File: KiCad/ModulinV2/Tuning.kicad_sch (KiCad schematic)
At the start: 35 parts, among them IC51 TL074HIDR

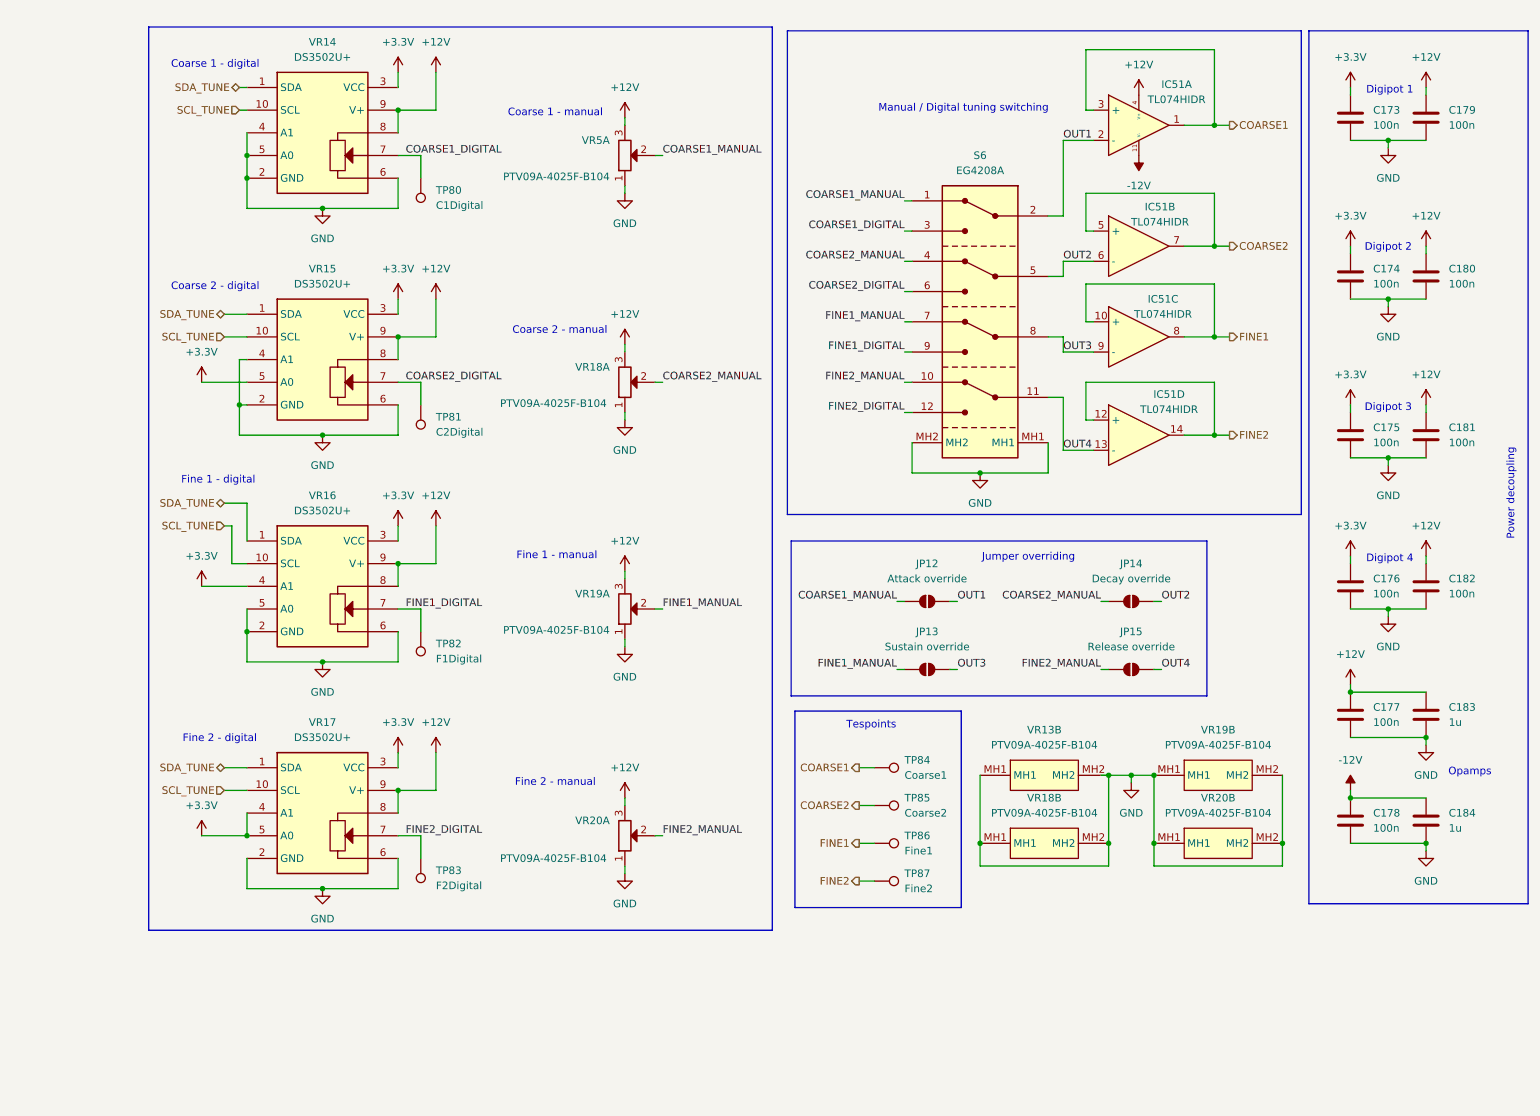
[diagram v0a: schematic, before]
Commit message: Finished routing MCU schematic, started with tuning
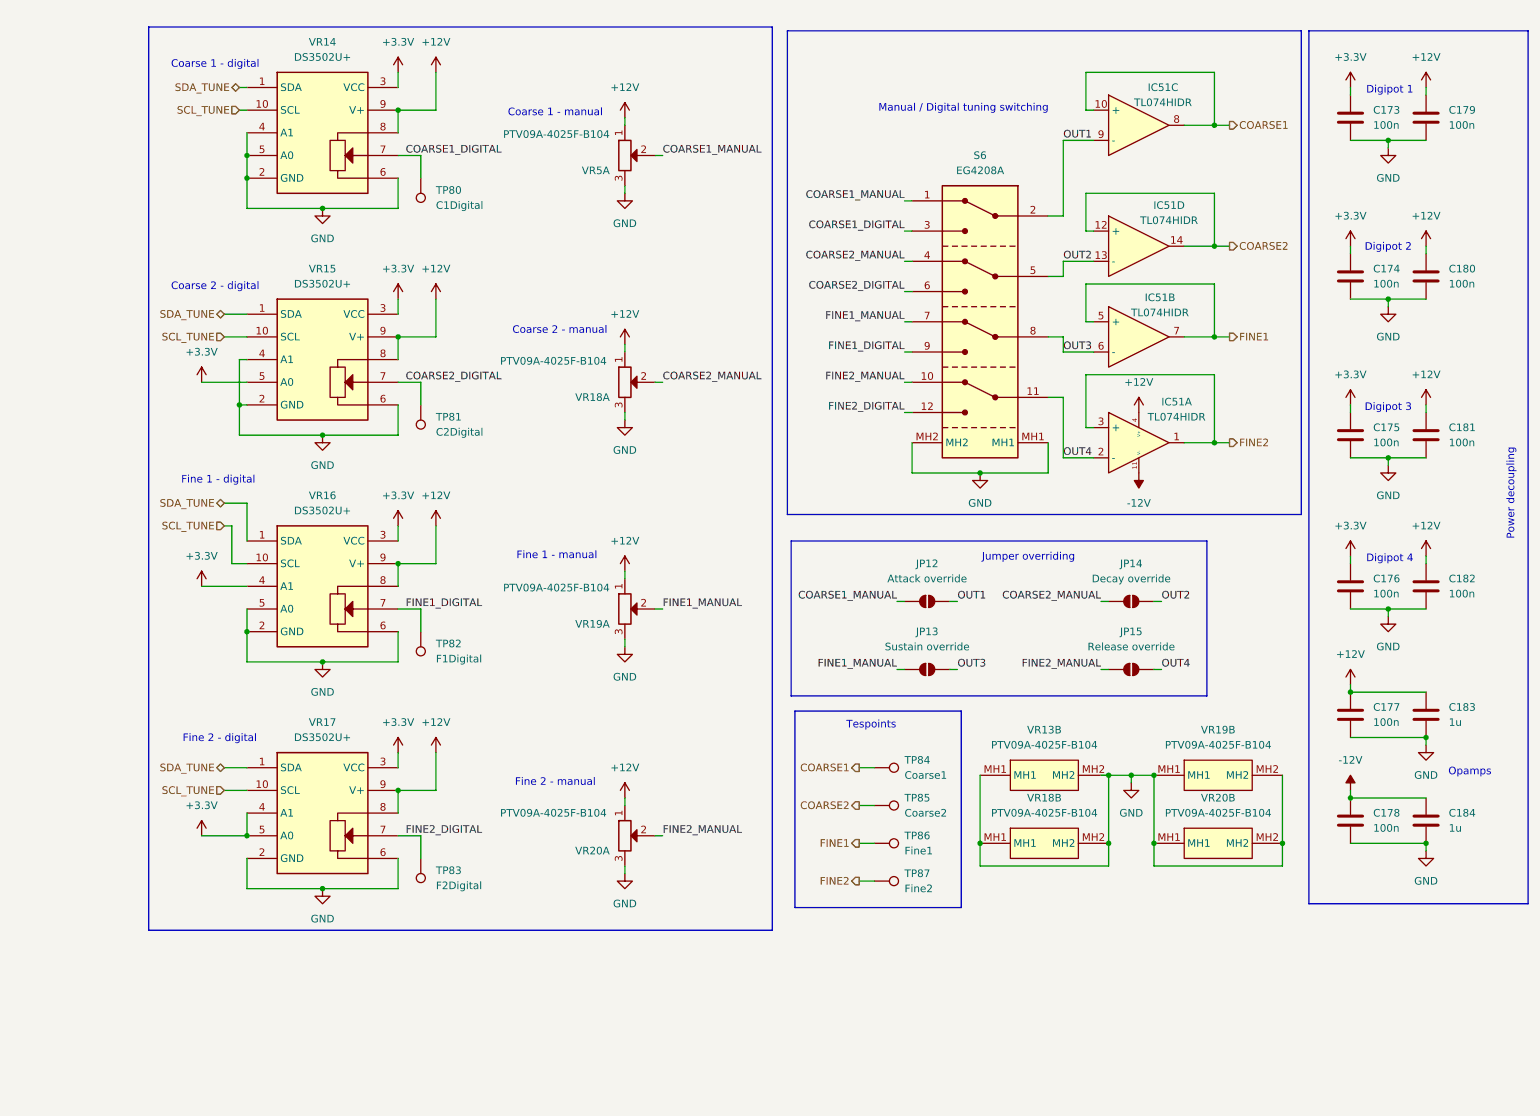
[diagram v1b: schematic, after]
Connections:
- net +12V: now also VR18.1, VR19.1, VR20.1, VR5.1; no longer VR18.3, VR19.3, VR20.3, VR5.3
- net COARSE1: now also IC51.10 (+), IC51.8; no longer IC51.1, IC51.3 (+)
- net COARSE2: now also IC51.12 (+), IC51.14; no longer IC51.5 (+), IC51.7
- net FINE1: now also IC51.5 (+), IC51.7; no longer IC51.10 (+), IC51.8
- net FINE2: now also IC51.1, IC51.3 (+); no longer IC51.12 (+), IC51.14
- net GND: now also VR18.3, VR19.3, VR20.3, VR5.3; no longer VR18.1, VR19.1, VR20.1, VR5.1
- net OUT1: now also IC51.9 (-); no longer IC51.2 (-)
- net OUT2: now also IC51.13 (-); no longer IC51.6 (-)
- net OUT3: now also IC51.6 (-); no longer IC51.9 (-)
- net OUT4: now also IC51.2 (-); no longer IC51.13 (-)
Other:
- moved on the sheet: IC51A, IC51B, IC51C, IC51D

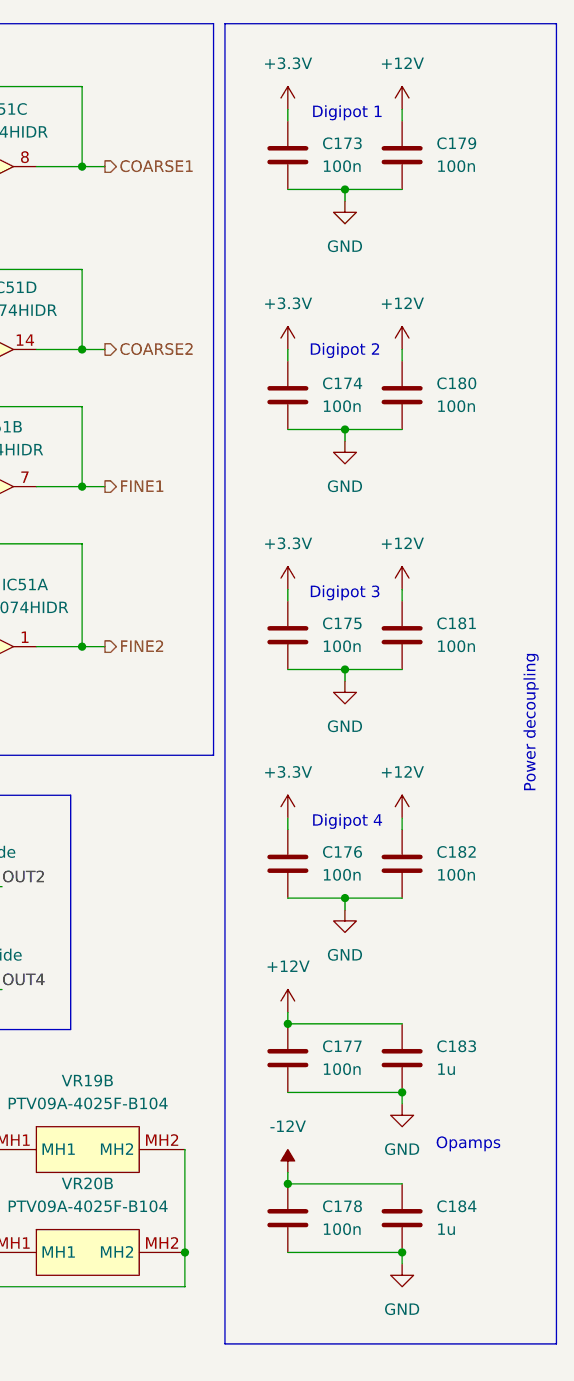
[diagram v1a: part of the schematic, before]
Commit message: Completed tuning & mod wheel layouts
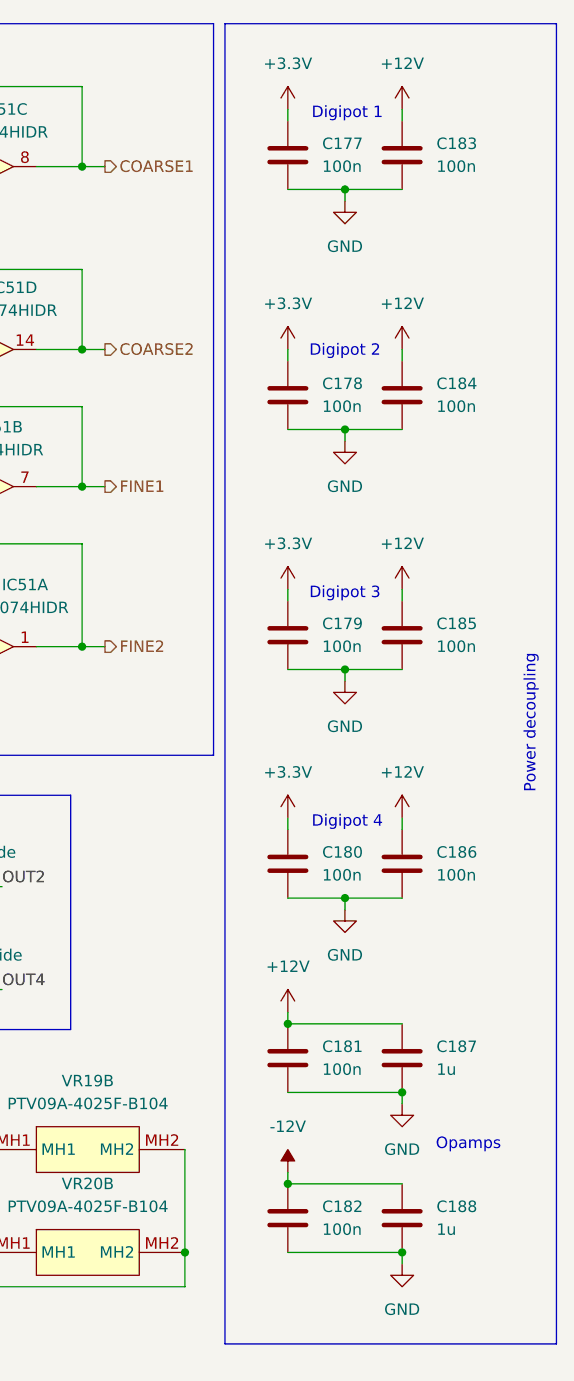
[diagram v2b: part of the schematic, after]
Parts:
- renumbered C173 to C177, C174 to C178, C175 to C179, C176 to C180, C177 to C181, C178 to C182, C179 to C183, C180 to C184, C181 to C185, C182 to C186, C183 to C187, C184 to C188

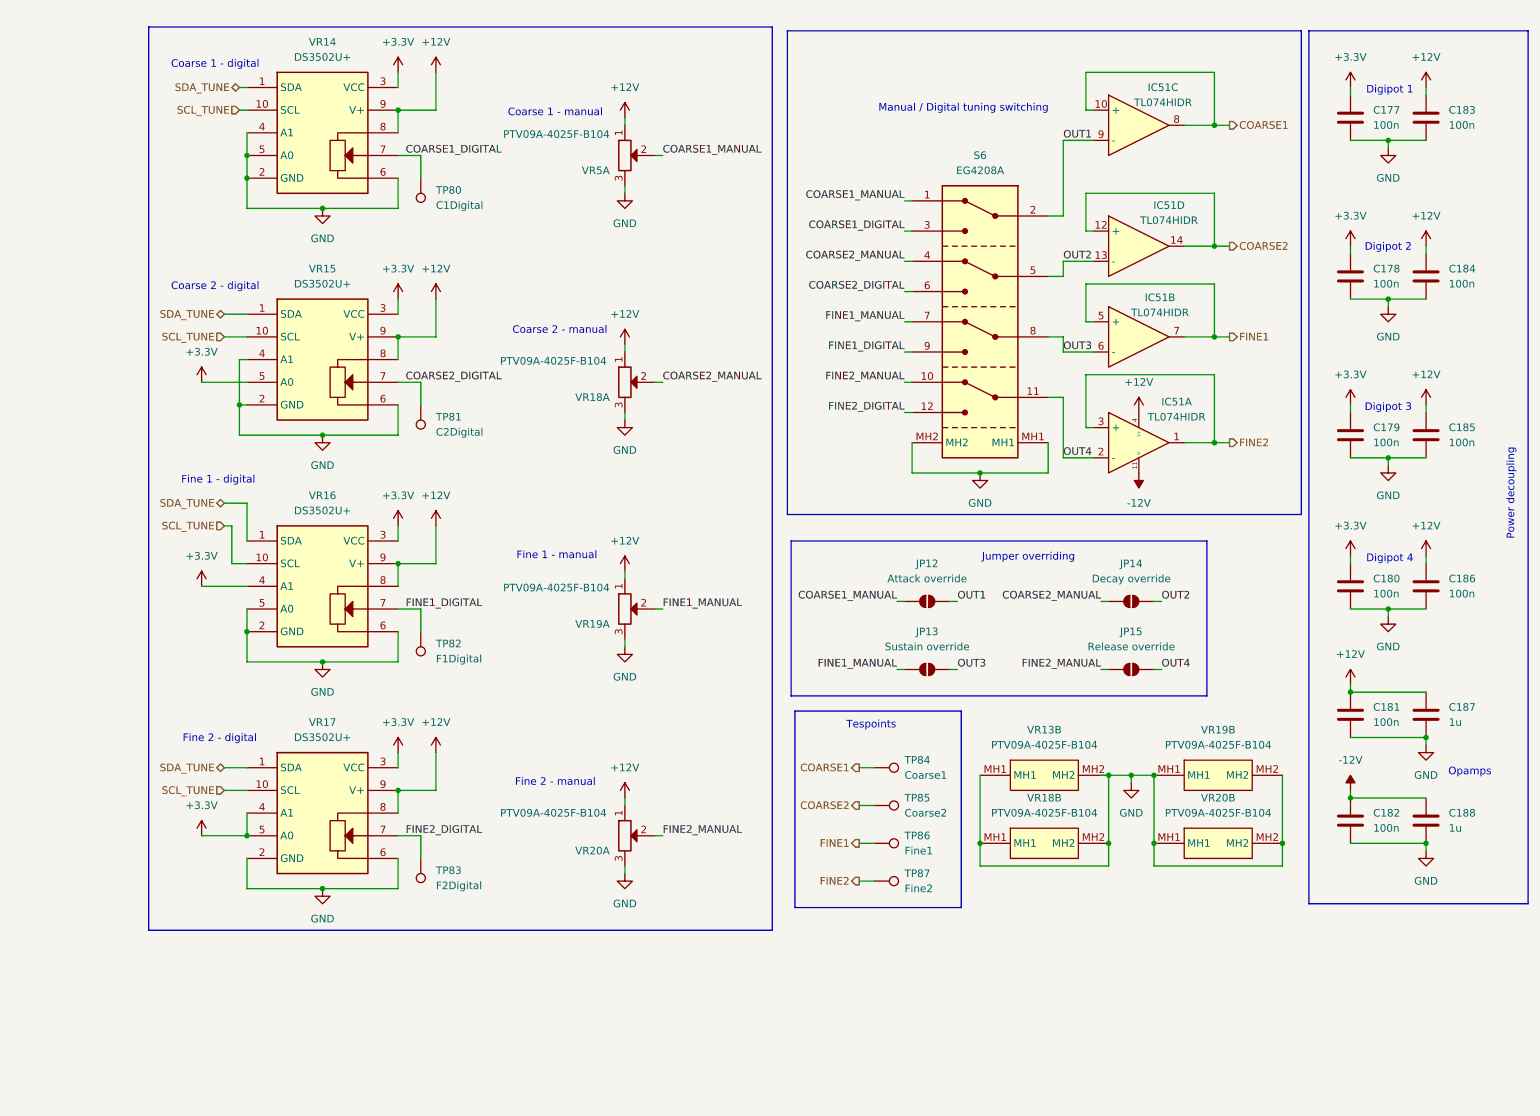
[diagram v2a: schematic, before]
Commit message: Fixed schematic connections
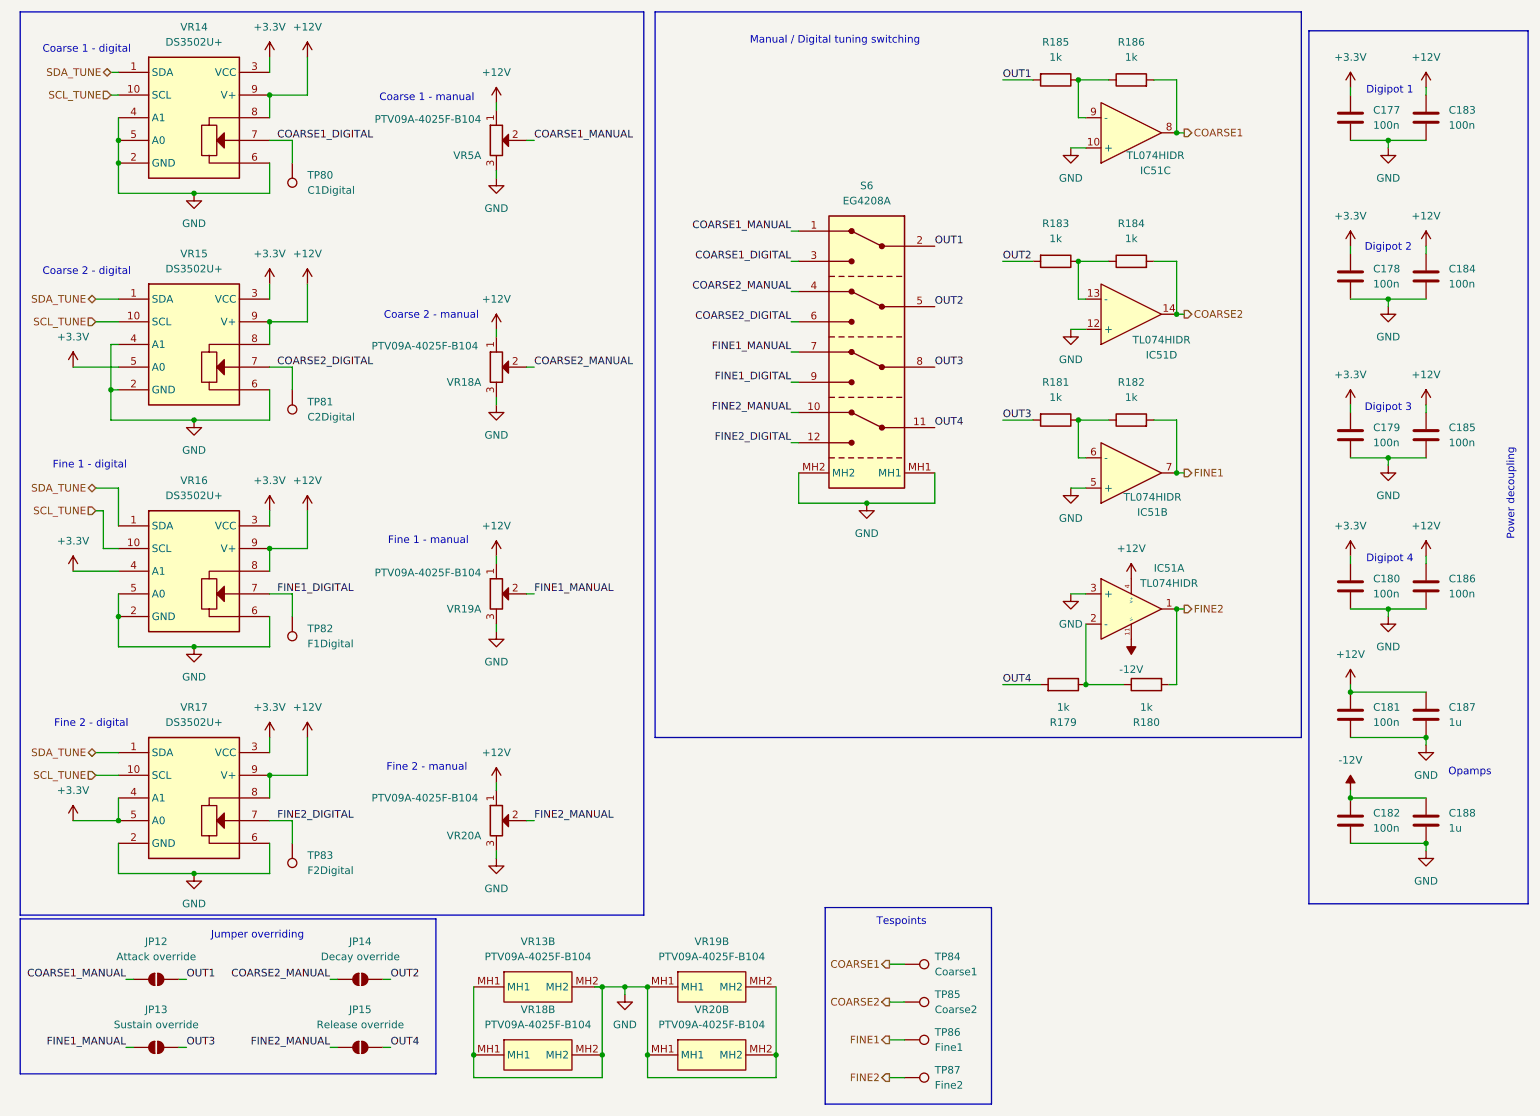
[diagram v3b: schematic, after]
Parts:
- added R179, R180, R181, R182, R183, R184, R185, R186: 1k, Resistor_SMD:R_0603_1608Metric_Pad0.98x0.95mm_HandSolder, symbol Device:R
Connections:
- net COARSE1: now also R186.2; no longer IC51.10 (+)
- net COARSE2: now also R184.2; no longer IC51.12 (+)
- net FINE1: now also R182.2; no longer IC51.5 (+)
- net FINE2: now also R180.2; no longer IC51.3 (+)
- net GND: now also IC51.10 (+), IC51.12 (+), IC51.3 (+), IC51.5 (+)
- net OUT1: now also R185.2; no longer IC51.9 (-)
- net OUT2: now also R183.2; no longer IC51.13 (-)
- net OUT3: now also R181.2; no longer IC51.6 (-)
- net OUT4: now also R179.2; no longer IC51.2 (-)
- new net: IC51.2 (-), R179.1, R180.1
- new net: IC51.9 (-), R185.1, R186.1
- new net: IC51.13 (-), R183.1, R184.1
- new net: IC51.6 (-), R181.1, R182.1
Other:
- company: (none) -> TalTech
- title: (none) -> Tuning
- moved on the sheet: IC51A, IC51B, IC51C, IC51D, JP12, JP13, JP14, JP15, S6, TP80, TP81, TP82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
